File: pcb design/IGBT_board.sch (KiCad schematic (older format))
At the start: 45 parts, among them Q1 IGBT, Q10 IGBT, Q11 IGBT, Q12 IGBT, Q2 IGBT, Q3 IGBT, Q4 IGBT, Q5 IGBT, Q6 IGBT, Q7 IGBT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

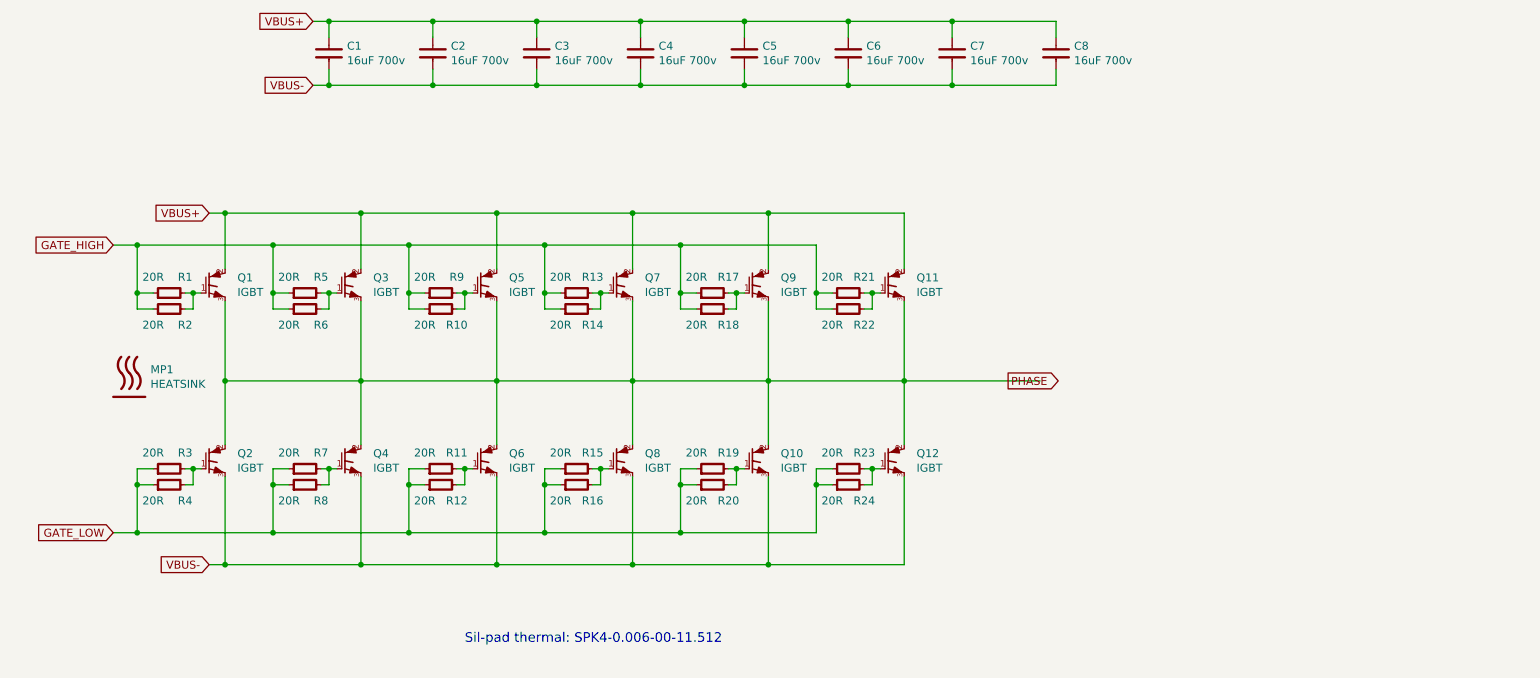
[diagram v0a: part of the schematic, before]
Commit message: Draft of bus bars and mounting points
Signed-off-by: Marcos Chaparro <mchaparro@paltatech.com>
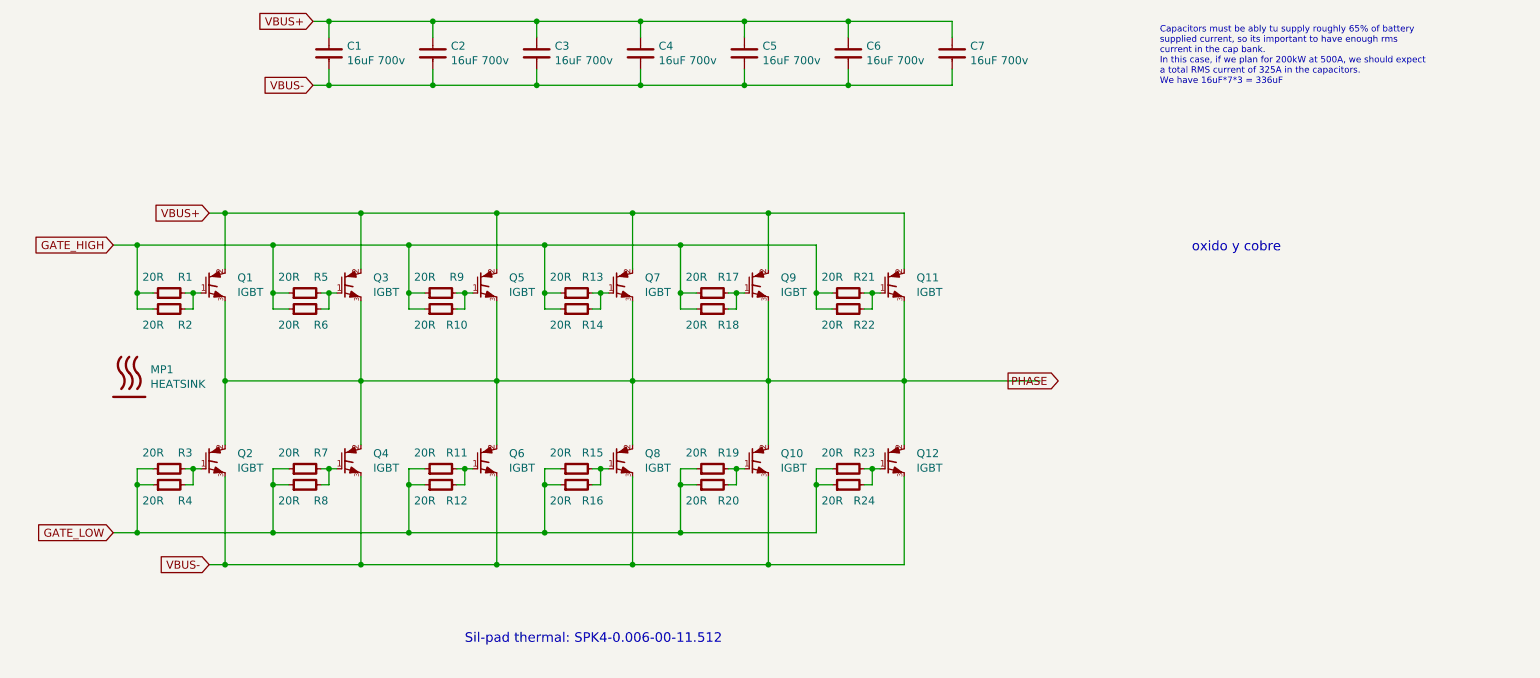
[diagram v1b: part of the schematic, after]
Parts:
- removed C8: 16uF 700v, paltatech:CAP_FILM_EPCOS_42x20mm, symbol C-FILM-6mm
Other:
- note added: "Capacitors must be ably tu supply roughly 65% of battery\nsupplied current, so its important to have enough rms\ncurrent in the cap bank.\nIn this case, if we plan for 200kW at 500A, we should expect\na total RMS current of 325A in the capacitors.\nWe have 16uF*7*3 = 336uF"
- note added: "oxido y cobre"
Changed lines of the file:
@@
 	2750 3650 2750 3550
 Wire Wire Line
-	2700 3550 2800 3550
+	2700 3550 2750 3550
+Wire Wire Line
+	2750 3550 2800 3550
 Connection ~ 2750 3550
 Wire Wire Line
 	2400 3650 2500 3650
 Wire Wire Line
-	2400 3250 2400 3650
+	2400 3250 2400 3550
+Wire Wire Line
+	2400 3550 2400 3650
 Wire Wire Line
 	2400 3550 2500 3550
@@
 	3600 3650 3600 3550
 Wire Wire Line
-	3550 3550 3650 3550
+	3550 3550 3600 3550
+Wire Wire Line
+	3600 3550 3650 3550
 Connection ~ 3600 3550
 Wire Wire Line
 	3250 3650 3350 3650
 Wire Wire Line
-	3250 3250 3250 3650
+	3250 3250 3250 3550
+Wire Wire Line
+	3250 3550 3250 3650
 Wire Wire Line
 	3250 3550 3350 3550
@@
 	2750 4750 2750 4650
 Wire Wire Line
-	2700 4650 2800 4650
+	2700 4650 2750 4650
+Wire Wire Line
+	2750 4650 2800 4650
 Connection ~ 2750 4650
 Wire Wire Line
 	2400 4750 2500 4750
 Wire Wire Line
-	2400 4650 2400 5050
+	2400 4650 2400 4750
+Wire Wire Line
+	2400 4750 2400 5050
 Wire Wire Line
 	2400 4650 2500 4650
@@
 	3600 4750 3600 4650
 Wire Wire Line
-	3550 4650 3650 4650
+	3550 4650 3600 4650
+Wire Wire Line
+	3600 4650 3650 4650
 Connection ~ 3600 4650
 Wire Wire Line
 	3250 4750 3350 4750
 Wire Wire Line
-	3250 5050 3250 4650
+	3250 5050 3250 4750
+Wire Wire Line
+	3250 4750 3250 4650
 Wire Wire Line
 	3250 4650 3350 4650
 Wire Wire Line
-	2950 3600 2950 4500
-Wire Wire Line
-	2950 4100 8050 4100
-Wire Wire Line
-	3800 3600 3800 4500
+	2950 3600 2950 4100
+Wire Wire Line
+	2950 4100 2950 4500
+Wire Wire Line
+	2950 4100 3800 4100
+Wire Wire Line
+	3800 4100 4650 4100
+Wire Wire Line
+	4650 4100 5500 4100
+Wire Wire Line
+	5500 4100 6350 4100
+Wire Wire Line
+	6350 4100 7200 4100
+Wire Wire Line
+	7200 4100 8050 4100
+Wire Wire Line
+	3800 3600 3800 4100
+Wire Wire Line
+	3800 4100 3800 4500
 Connection ~ 2950 4100
 Connection ~ 3800 4100
@@
 Connection ~ 3250 3550
 Wire Wire Line
-	6650 5050 2250 5050
+	6650 5050 5800 5050
+Wire Wire Line
+	5800 5050 4950 5050
+Wire Wire Line
+	4950 5050 4100 5050
+Wire Wire Line
+	4100 5050 3250 5050
+Wire Wire Line
+	3250 5050 2400 5050
+Wire Wire Line
+	2400 5050 2250 5050
 Connection ~ 2400 4750
 Connection ~ 3250 4750
 Wire Wire Line
-	2250 3250 6650 3250
-Wire Wire Line
-	2850 5250 7200 5250
-Wire Wire Line
-	2850 3050 7200 3050
+	2250 3250 2400 3250
+Wire Wire Line
+	2400 3250 3250 3250
+Wire Wire Line
+	3250 3250 4100 3250
+Wire Wire Line
+	4100 3250 4950 3250
+Wire Wire Line
+	4950 3250 5800 3250
+Wire Wire Line
+	5800 3250 6650 3250
+Wire Wire Line
+	2850 5250 2950 5250
+Wire Wire Line
+	2950 5250 3800 5250
+Wire Wire Line
+	3800 5250 4650 5250
+Wire Wire Line
+	4650 5250 5500 5250
+Wire Wire Line
+	5500 5250 6350 5250
+Wire Wire Line
+	6350 5250 7200 5250
+Wire Wire Line
+	2850 3050 2950 3050
+Wire Wire Line
+	2950 3050 3800 3050
+Wire Wire Line
+	3800 3050 4650 3050
+Wire Wire Line
+	4650 3050 5500 3050
+Wire Wire Line
+	5500 3050 6350 3050
+Wire Wire Line
+	6350 3050 7200 3050
 $Comp
 L IGBT Q5
@@
 	4450 3650 4450 3550
 Wire Wire Line
-	4400 3550 4500 3550
+	4400 3550 4450 3550
+Wire Wire Line
+	4450 3550 4500 3550
 Connection ~ 4450 3550
 Wire Wire Line
 	4100 3650 4200 3650
 Wire Wire Line
-	4100 3250 4100 3650
+	4100 3250 4100 3550
+Wire Wire Line
+	4100 3550 4100 3650
 Wire Wire Line
 	4100 3550 4200 3550
@@
 	5300 3650 5300 3550
 Wire Wire Line
-	5250 3550 5350 3550
+	5250 3550 5300 3550
+Wire Wire Line
+	5300 3550 5350 3550
 Connection ~ 5300 3550
 Wire Wire Line
 	4950 3650 5050 3650
 Wire Wire Line
-	4950 3250 4950 3650
+	4950 3250 4950 3550
+Wire Wire Line
+	4950 3550 4950 3650
 Wire Wire Line
 	4950 3550 5050 3550
@@
 	4450 4750 4450 4650
 Wire Wire Line
-	4400 4650 4500 4650
+	4400 4650 4450 4650
+Wire Wire Line
+	4450 4650 4500 4650
 Connection ~ 4450 4650
 Wire Wire Line
 	4100 4750 4200 4750
 Wire Wire Line
-	4100 4650 4100 5050
+	4100 4650 4100 4750
+Wire Wire Line
+	4100 4750 4100 5050
 Wire Wire Line
 	4100 4650 4200 4650
@@
 	5300 4750 5300 4650
 Wire Wire Line
-	5250 4650 5350 4650
+	5250 4650 5300 4650
+Wire Wire Line
+	5300 4650 5350 4650
 Connection ~ 5300 4650
 Wire Wire Line
 	4950 4750 5050 4750
 Wire Wire Line
-	4950 4650 4950 5050
+	4950 4650 4950 4750
+Wire Wire Line
+	4950 4750 4950 5050
 Wire Wire Line
 	4950 4650 5050 4650
 Wire Wire Line
-	4650 3600 4650 4500
-Wire Wire Line
-	5500 3600 5500 4500
+	4650 3600 4650 4100
+Wire Wire Line
+	4650 4100 4650 4500
+Wire Wire Line
+	5500 3600 5500 4100
+Wire Wire Line
+	5500 4100 5500 4500
 Connection ~ 4650 4100
 Connection ~ 5500 4100
@@
 	6150 3650 6150 3550
 Wire Wire Line
-	6100 3550 6200 3550
+	6100 3550 6150 3550
+Wire Wire Line
+	6150 3550 6200 3550
 Connection ~ 6150 3550
 Wire Wire Line
 	5800 3650 5900 3650
 Wire Wire Line
-	5800 3250 5800 3650
+	5800 3250 5800 3550
+Wire Wire Line
+	5800 3550 5800 3650
 Wire Wire Line
 	5800 3550 5900 3550
@@
 	7000 3650 7000 3550
 Wire Wire Line
-	6950 3550 7050 3550
+	6950 3550 7000 3550
+Wire Wire Line
+	7000 3550 7050 3550
 Connection ~ 7000 3550
 Wire Wire Line
 	6650 3650 6750 3650
 Wire Wire Line
-	6650 3250 6650 3650
+	6650 3250 6650 3550
+Wire Wire Line
+	6650 3550 6650 3650
 Wire Wire Line
 	6650 3550 6750 3550
@@
 	6150 4750 6150 4650
 Wire Wire Line
-	6100 4650 6200 4650
+	6100 4650 6150 4650
+Wire Wire Line
+	6150 4650 6200 4650
 Connection ~ 6150 4650
 Wire Wire Line
 	5800 4750 5900 4750
 Wire Wire Line
-	5800 4650 5800 5050
+	5800 4650 5800 4750
+Wire Wire Line
+	5800 4750 5800 5050
 Wire Wire Line
 	5800 4650 5900 4650
@@
 	7000 4750 7000 4650
 Wire Wire Line
-	6950 4650 7050 4650
+	6950 4650 7000 4650
+Wire Wire Line
+	7000 4650 7050 4650
 Connection ~ 7000 4650
 Wire Wire Line
 	6650 4750 6750 4750
 Wire Wire Line
-	6650 4650 6650 5050
+	6650 4650 6650 4750
+Wire Wire Line
+	6650 4750 6650 5050
 Wire Wire Line
 	6650 4650 6750 4650
 Wire Wire Line
-	6350 3600 6350 4500
-Wire Wire Line
-	7200 3600 7200 4500
+	6350 3600 6350 4100
+Wire Wire Line
+	6350 4100 6350 4500
+Wire Wire Line
+	7200 3600 7200 4100
+Wire Wire Line
+	7200 4100 7200 4500
 Connection ~ 6350 4100
 Connection ~ 7200 4100
@@
 	1    0    0    -1
 $EndComp
-$Comp
-L C-FILM-6mm C8
-U 1 1 5813A296
-P 8150 2050
-F 0 "C8" H 8263 2096 50  0000 L CNN
-F 1 "16uF 700v" H 8263 2005 50  0000 L CNN
-F 2 "paltatech:CAP_FILM_EPCOS_42x20mm" H 8150 2050 50  0001 C CNN
-F 3 "" H 8140 2025 60  0000 C CNN
-F 4 "B32796G3166K" H 8150 2050 60  0001 C CNN "mfg#"
-	1    8150 2050
-	1    0    0    -1
-$EndComp
 Wire Wire Line
 	3600 1950 3600 1850
 Wire Wire Line
-	3500 1850 8150 1850
+	3500 1850 3600 1850
+Wire Wire Line
+	3600 1850 4250 1850
+Wire Wire Line
+	4250 1850 4900 1850
+Wire Wire Line
+	4900 1850 5550 1850
+Wire Wire Line
+	5550 1850 6200 1850
+Wire Wire Line
+	6200 1850 6850 1850
+Wire Wire Line
+	6850 1850 7500 1850
 Wire Wire Line
 	4250 1850 4250 1950
@@
 Connection ~ 6850 1850
 Wire Wire Line
-	8150 1850 8150 1950
-Connection ~ 7500 1850
-Wire Wire Line
-	8150 2250 8150 2150
-Wire Wire Line
-	3500 2250 8150 2250
+	3500 2250 3600 2250
+Wire Wire Line
+	3600 2250 4250 2250
+Wire Wire Line
+	4250 2250 4900 2250
+Wire Wire Line
+	4900 2250 5550 2250
+Wire Wire Line
+	5550 2250 6200 2250
+Wire Wire Line
+	6200 2250 6850 2250
+Wire Wire Line
+	6850 2250 7500 2250
 Wire Wire Line
 	7500 2250 7500 2150
 Wire Wire Line
 	6850 2250 6850 2150
-Connection ~ 7500 2250
 Wire Wire Line
 	6200 2250 6200 2150
@@
 Text Notes 4450 5750 0    60   ~ 0
 Sil-pad thermal: SPK4-0.006-00-11.512
+Text Notes 8800 2250 0    40   ~ 0
+Capacitors must be ably tu supply roughly 65% of battery\nsupplied current, so its important to have enough rms\ncurrent in the cap bank.\nIn this case, if we plan for 200kW at 500A, we should expect\na total RMS current of 325A in the capacitors.\nWe have 16uF*7*3 = 336uF
+Text Notes 9000 3300 0    60   ~ 0
+oxido y cobre
 $EndSCHEMATC

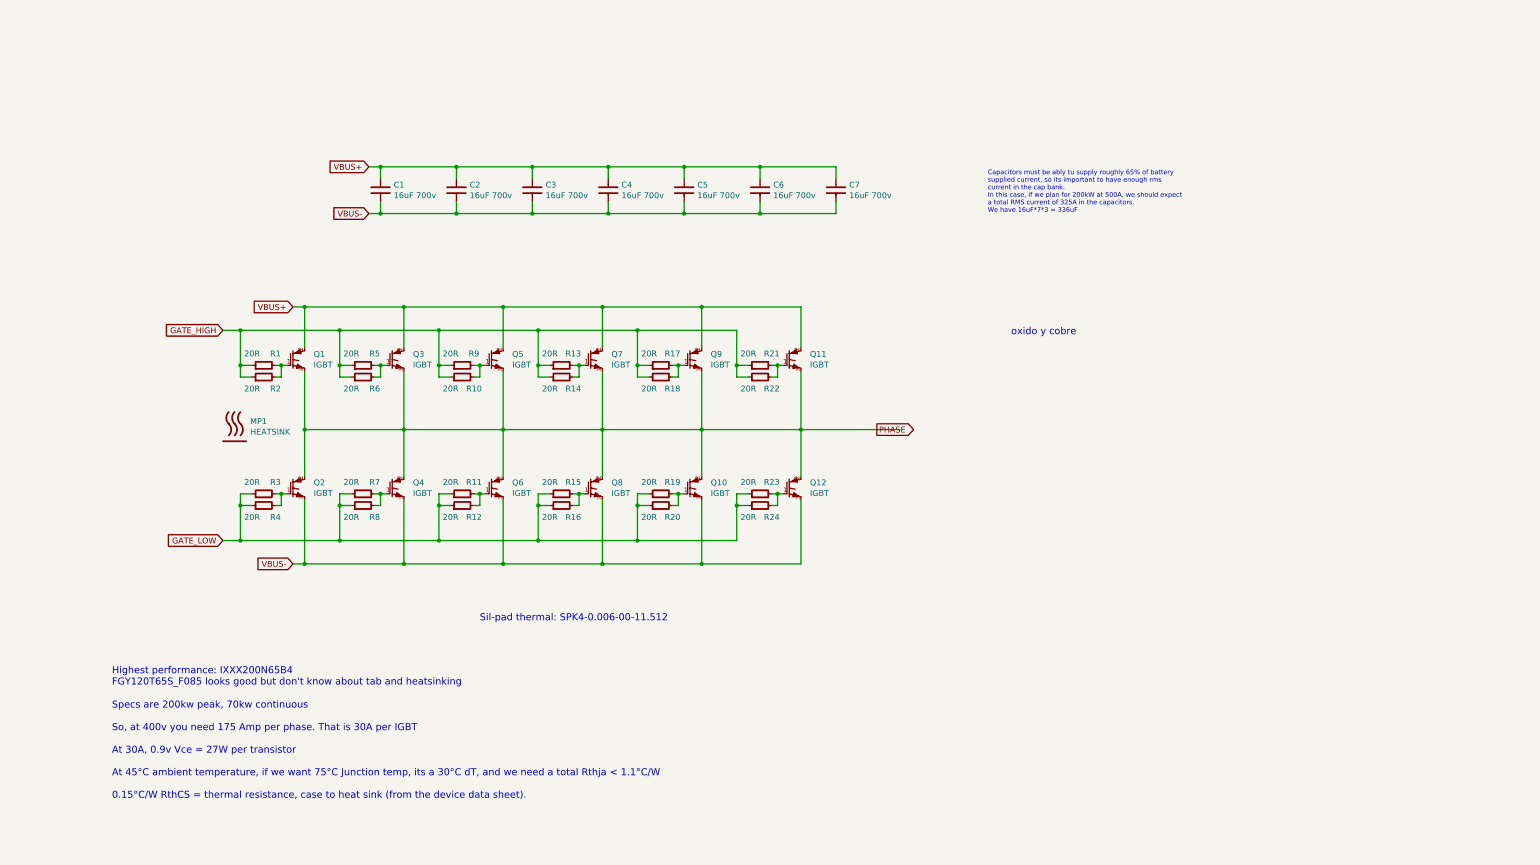
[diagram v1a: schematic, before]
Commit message: Added IGBT gate driver circuit and isolated power supply
Signed-off-by: Marcos Chaparro <mchaparro@paltatech.com>
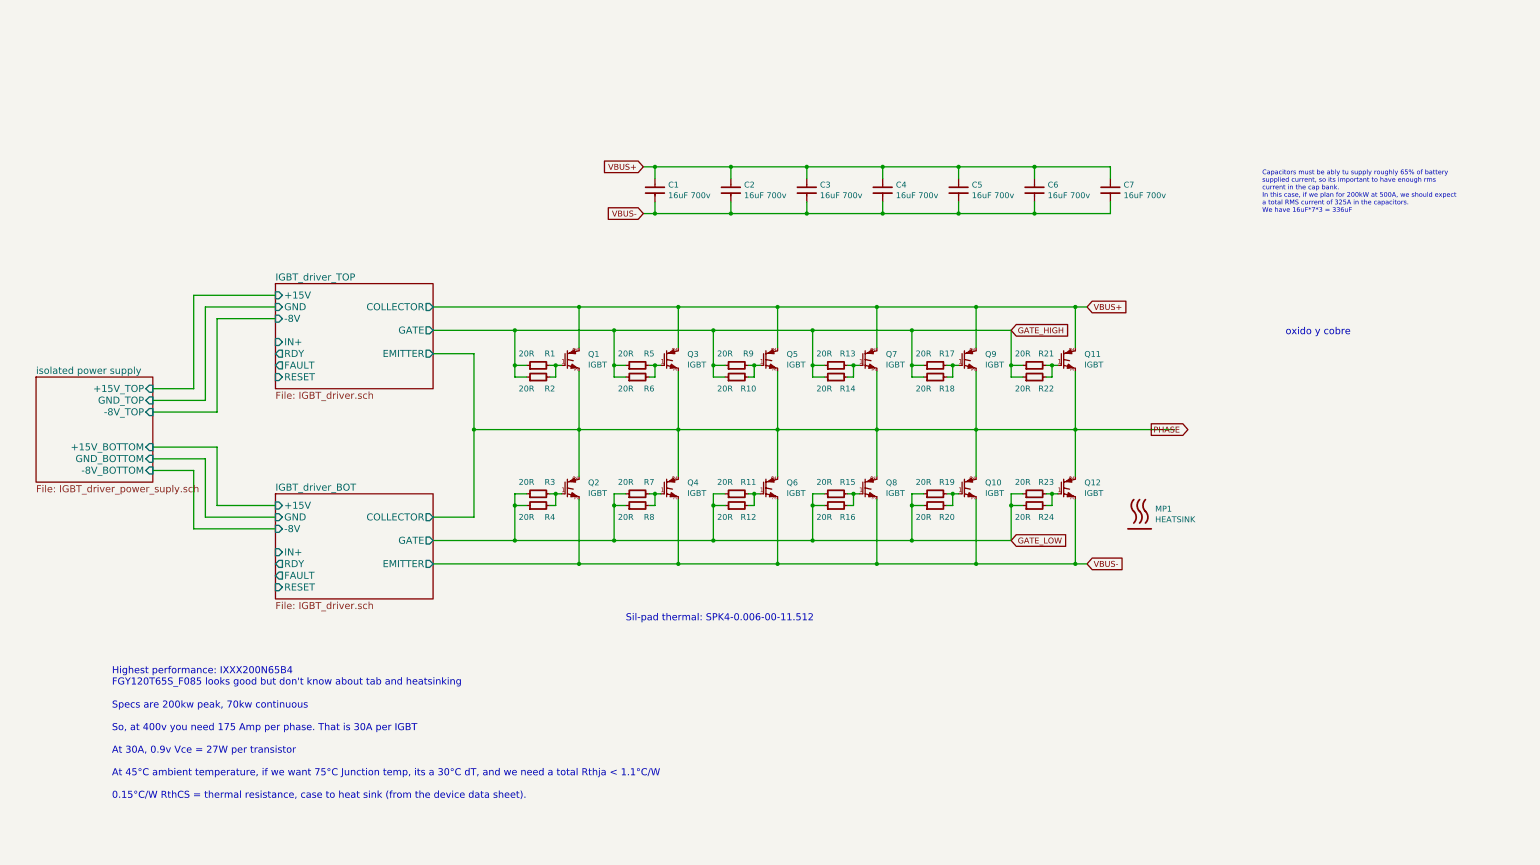
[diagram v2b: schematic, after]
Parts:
- Q1: mfg# IXXH80N65B4-ND -> IXXX110N65B4H1
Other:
- moved on the sheet: C1, C2, C3, C4, C5, C6, C7, MP1, Q1, Q10, Q11, Q12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
